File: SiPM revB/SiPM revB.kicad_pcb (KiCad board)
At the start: 4 copper layers, 55.6 x 69 mm, 150 parts, among them Q1 MountingHole_Pad, Q2 MountingHole_Pad, Q3 MountingHole_Pad, Q4 MountingHole_Pad

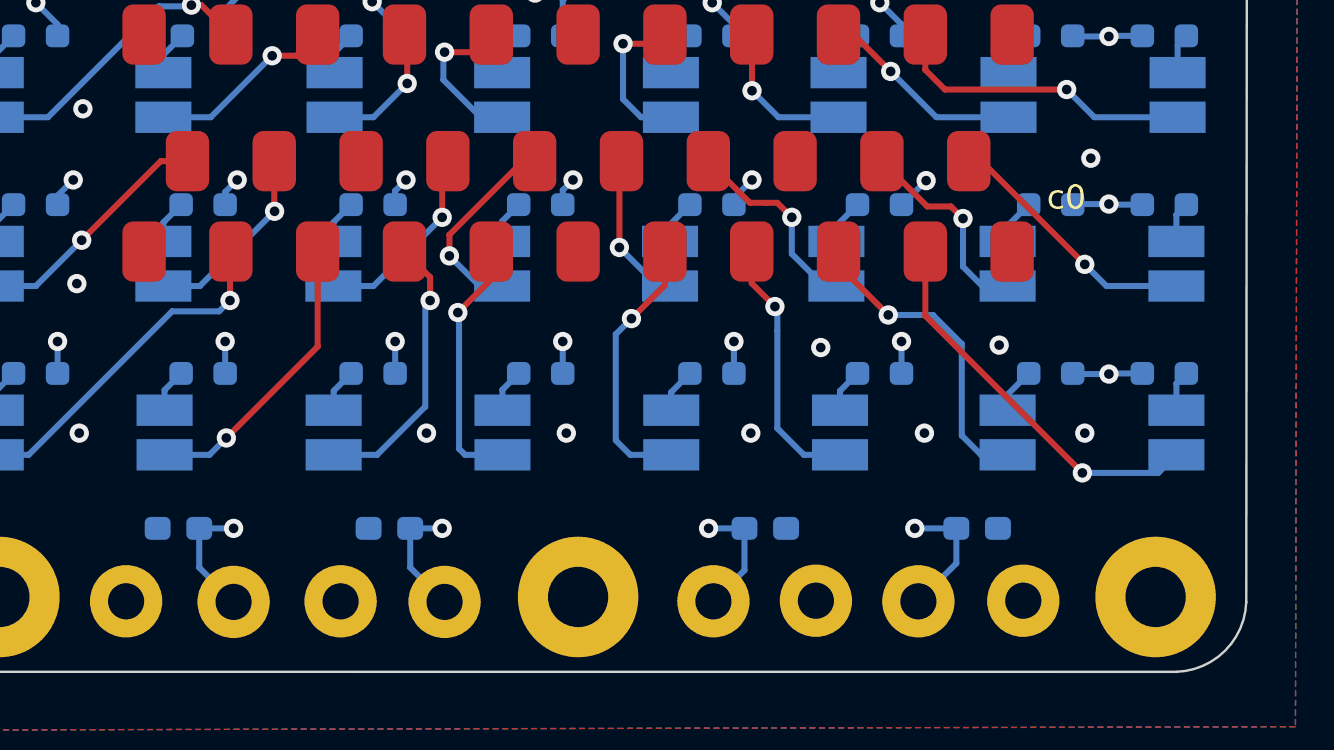
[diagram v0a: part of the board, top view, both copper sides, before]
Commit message: Added RevB and removed 3/4 caps at HV and added 4 caps in Q4 for filtering
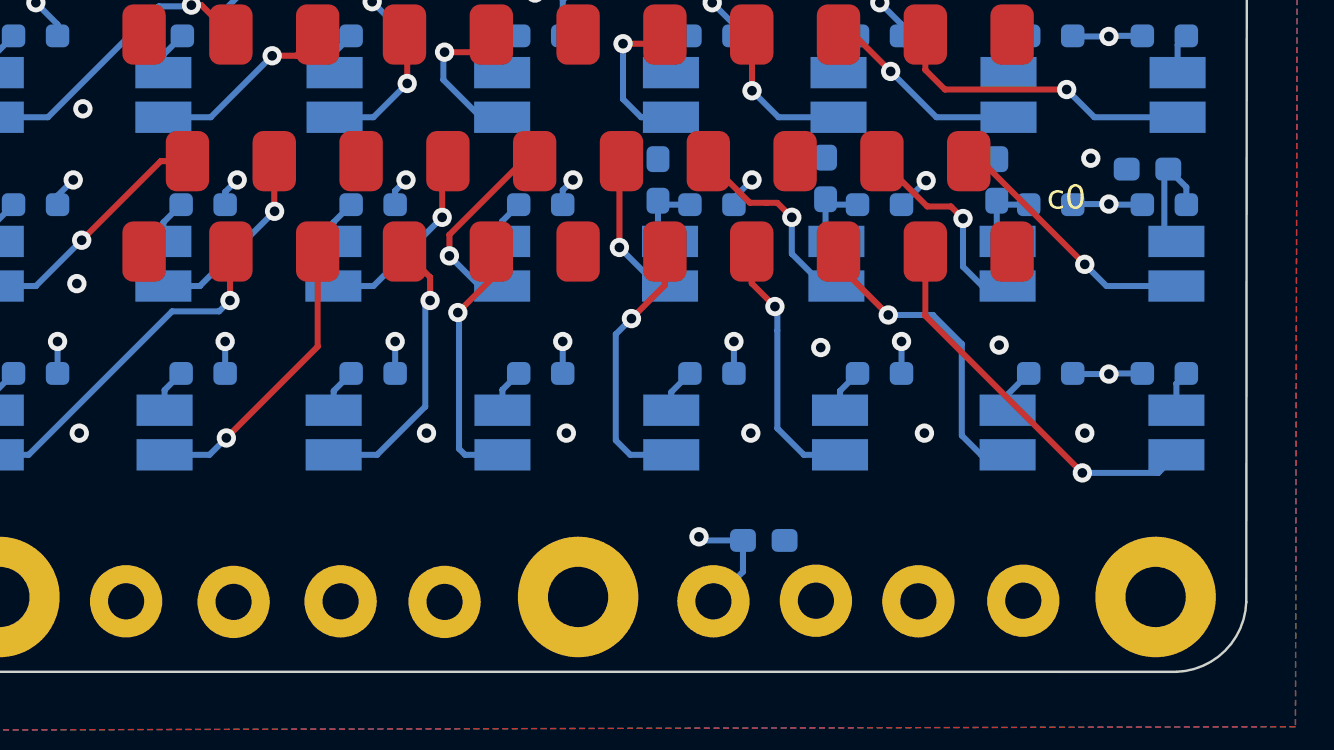
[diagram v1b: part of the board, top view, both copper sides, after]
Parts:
- added C8: 220pF, Capacitor_SMD:C_0603_1608Metric_Pad1.08x0.95mm_HandSolder, B.Cu at (154.6, 124.1)
- C4, C5, C6, C7: value 220pF -> 0.1 uF
- moved C4 24.6 mm to (150.2, 109.2), turned to -90 degrees
- moved C5 23.2 mm to (157.2, 109.1), turned to -90 degrees
- moved C7 21.8 mm to (170.5, 108.7), turned to 0 degrees
- moved C6 14.5 mm to (164.2, 109.2), turned to -90 degrees
- renumbered Q1 to H11, Q2 to H12, Q4 to H13, Q3 to H14
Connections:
- C4 pad 1: +BATT 3 -> GND
- C4 pad 2: GND -> Net-(D57-K)
- C5 pad 1: +BATT 2 -> GND
- C5 pad 2: GND -> Net-(D59-K)
- C6 pad 2: +BATT 4 -> Net-(D61-K)
- C7 pad 2: +BATT 1 -> Net-(D63-K)
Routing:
- net +BATT 2: track 62.8 -> 59.2 mm, vias 17 -> 16
- net Net-(D63-K): track 1.70 -> 5.06 mm
- net +BATT 4: track 31.7 -> 28.8 mm, vias 13 -> 12
- net +BATT 3: track 30.9 -> 28.9 mm, vias 17 -> 16
- net Net-(D59-K): track 1.89 -> 3.35 mm
- net Net-(D57-K): track 1.87 -> 3.29 mm
- net Net-(D61-K): track 1.89 -> 3.27 mm
